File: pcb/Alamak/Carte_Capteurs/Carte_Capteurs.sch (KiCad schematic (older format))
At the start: 36 parts, among them J13 Conn_01x02, J5 Conn_02x07_Odd_Even, J6 Molex KK 254, J7 Samtec FTS-105-01-L-DV, J8 Samtec FTS-105-01-L-DV, Q1 NTR3C21NZT1G, SW1 SMR8016C-1, SW2 Reset, SW3 USER1, SW4 USER2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

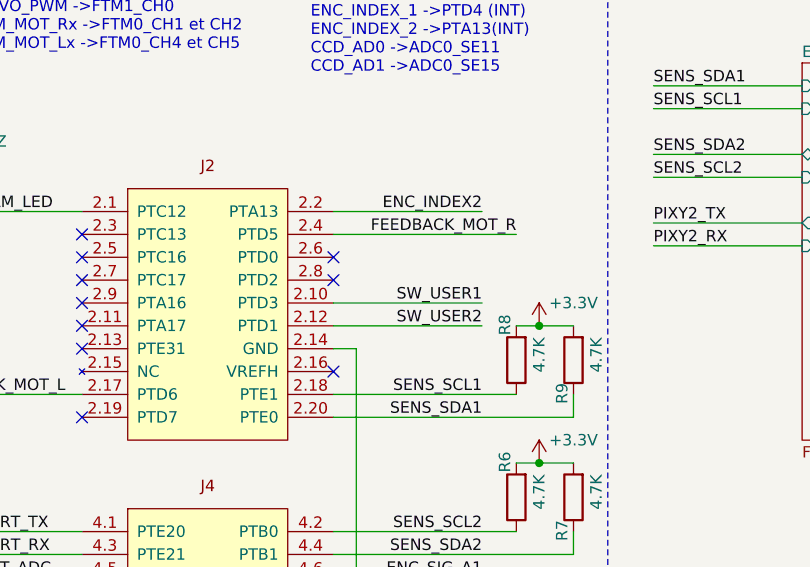
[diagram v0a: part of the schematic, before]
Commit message: Ajout des regles NXP Cup pour 2020 (V1) + modifs mineures sur pcbs
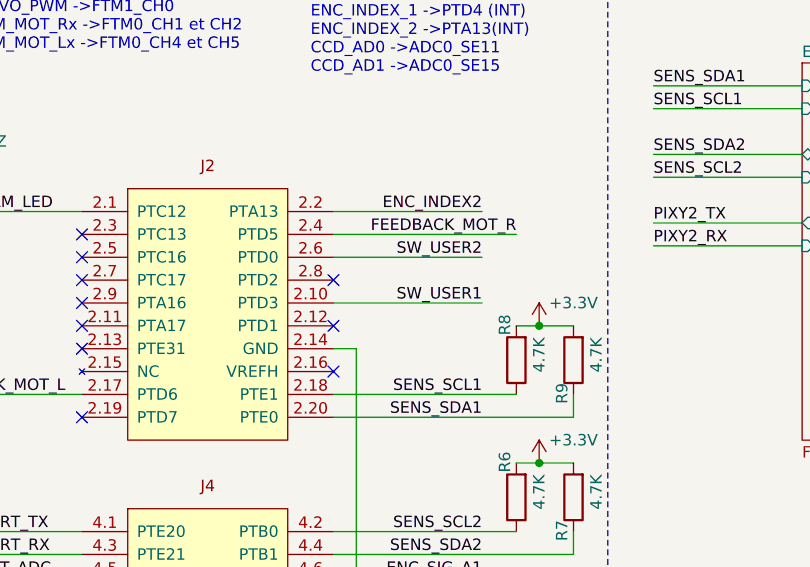
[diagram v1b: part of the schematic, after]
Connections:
- net SW_USER2: now also U1.2.6 (PTD0); no longer U1.2.12 (PTD1)
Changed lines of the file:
@@
 	1500 6900 800  6900
-Wire Wire Line
-	4800 5400 5450 5400
 Wire Wire Line
 	4800 5300 5450 5300
 Text Label 5450 5300 2    50   ~ 0
 SW_USER1
-Text Label 5450 5400 2    50   ~ 0
+Text Label 5450 5100 2    50   ~ 0
 SW_USER2
 Wire Wire Line
@@
 NoConn ~ 2600 6300
 NoConn ~ 1500 5600
-NoConn ~ 4800 5100
 NoConn ~ 4800 5200
 NoConn ~ 4800 5600
@@
 Text Label 6200 5050 0    50   ~ 0
 PIXY2_RX
+Wire Wire Line
+	4800 5100 5450 5100
+NoConn ~ 4800 5400
 $EndSCHEMATC
